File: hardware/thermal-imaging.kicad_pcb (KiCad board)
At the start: 2 copper layers, 40 x 40 mm, 47 parts, among them P1 CON-SENSOR, P2 Boot, P3 Debug, Q1 Oscillator, U1 XMC1XXX24, U10 DRILL, U11 DRILL, U2 74LVC1G17, U3 74LVC1G17, U4 FLIR-Lepton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

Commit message: specify oscillator frequency
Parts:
- Q1: value Oscillator -> 25MHz
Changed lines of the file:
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@@
-(kicad_pcb (version 4) (host pcbnew 4.0.2+dfsg1-stable)
+(kicad_pcb (version 4) (host pcbnew 4.0.6-e0-6349~52~ubuntu16.10.1)
   (general
     (links 145)
     (no_connects 0)
-    (area 166.324999 80.824999 206.475001 120.975001)
+    (area 165.544999 80.044999 282.34286 161.24)
     (thickness 1.6)
     (drawings 12)
@@
       (effects (font (size 0.3 0.3) (thickness 0.075)))
     )
-    (fp_text value Oscillator (at 0 -0.5 270) (layer F.Fab)
+    (fp_text value 25MHz (at 0 -0.5 270) (layer F.Fab)
       (effects (font (size 0.3 0.3) (thickness 0.075)))
     )

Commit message: specify filter circuit
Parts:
- C16: value TBD -> 220pF
- RP1: value TBD -> 82
- U7: value MCP1700T-1202E/TT -> MCP1700T-1202E/TT
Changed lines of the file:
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@@
-(kicad_pcb (version 4) (host pcbnew 4.0.6-e0-6349~52~ubuntu16.10.1)
+(kicad_pcb (version 4) (host pcbnew 4.0.7-e0-6372~58~ubuntu16.10.1)
   (general
     (links 145)
     (no_connects 0)
-    (area 165.544999 80.044999 282.34286 161.24)
+    (area 166.324999 80.824999 206.475001 120.975001)
     (thickness 1.6)
     (drawings 12)
@@
       (effects (font (size 0.3 0.3) (thickness 0.075)))
     )
-    (fp_text value " MCP1700T-1202E/TT " (at -0.775 -1.15) (layer F.Fab)
+    (fp_text value MCP1700T-1202E/TT (at -0.775 -1.15) (layer F.Fab)
       (effects (font (size 0.29972 0.29972) (thickness 0.07112)))
     )
@@
       (effects (font (size 0.2 0.2) (thickness 0.05)))
     )
-    (fp_text value TBD (at -0.025 -0.45 225) (layer F.Fab)
+    (fp_text value 82 (at -0.025 -0.45 225) (layer F.Fab)
       (effects (font (size 0.2 0.2) (thickness 0.05)))
     )
@@
       (effects (font (size 0.2 0.2) (thickness 0.05)))
     )
-    (fp_text value TBD (at 0 -0.275 315) (layer F.Fab)
+    (fp_text value 220pF (at 0 -0.275 315) (layer F.Fab)
       (effects (font (size 0.2 0.2) (thickness 0.05)))
     )

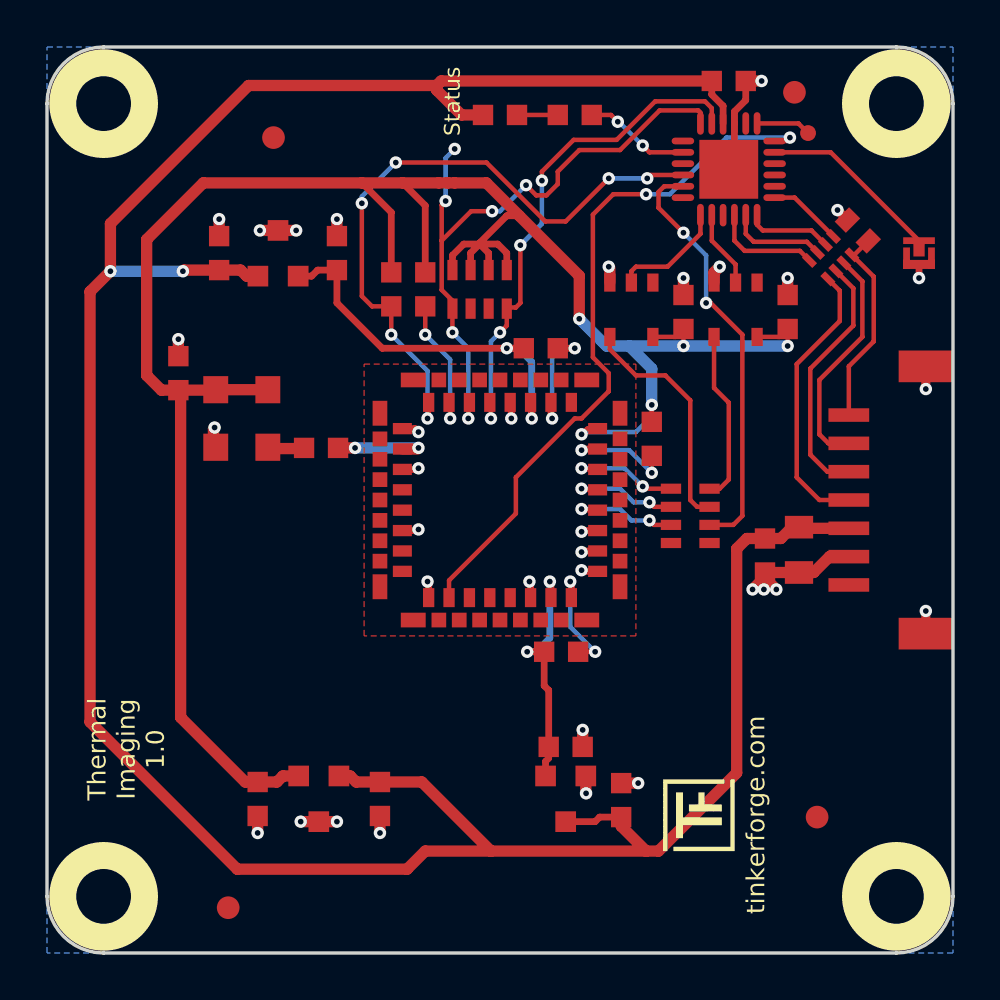
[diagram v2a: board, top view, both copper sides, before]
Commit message: add flir logo
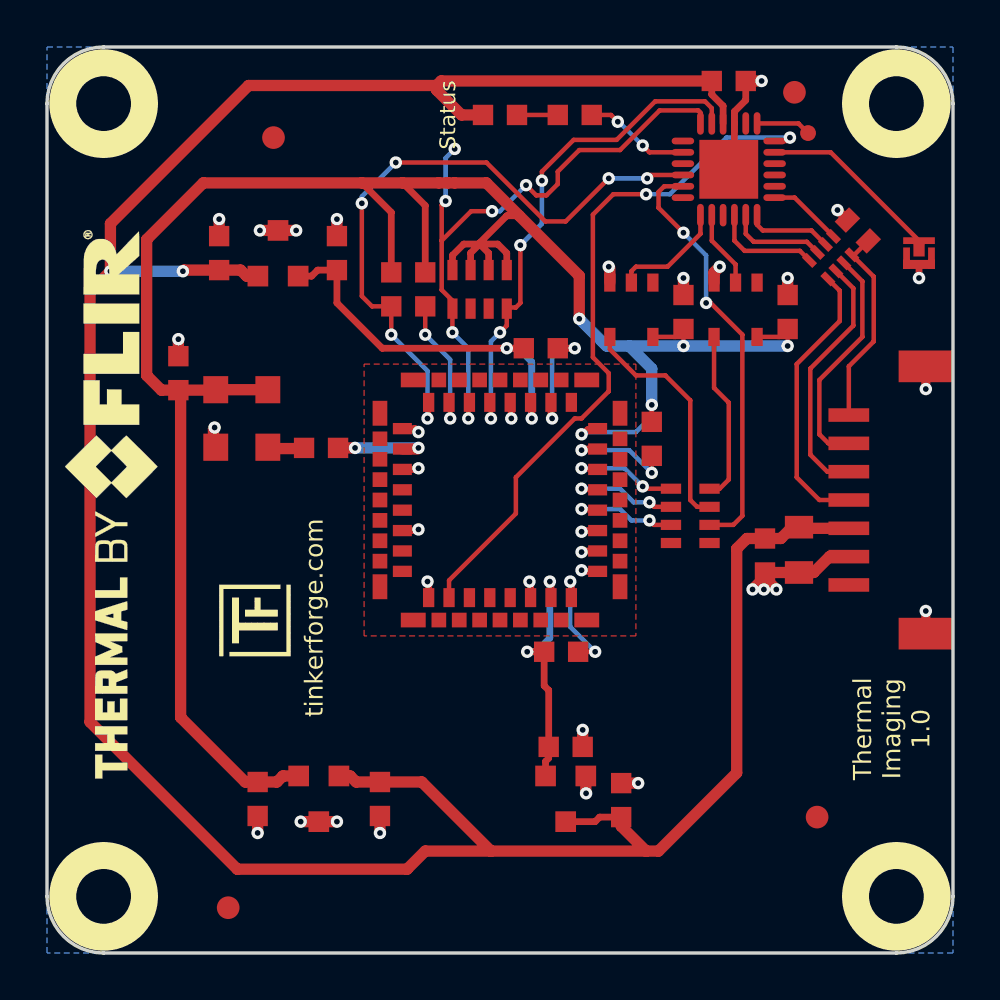
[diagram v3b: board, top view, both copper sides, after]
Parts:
- added G***: LOGO, kicad-libraries:logo_therm_by_flir, F.Cu at (169.2, 100.9)
- U5, U6: value AP7333-28 -> AP7333-28SAG
- moved G*** 21.4 mm to (174.0, 107.8)

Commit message: specify processor type
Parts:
- U1: value XMC1XXX24 -> XMC1302-32
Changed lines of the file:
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@@
     (links 145)
     (no_connects 0)
-    (area 166.324999 80.824999 206.475001 120.975001)
+    (area 165.544999 80.044999 282.34286 161.24)
     (thickness 1.6)
     (drawings 12)
@@
       (effects (font (size 0.3 0.3) (thickness 0.075)))
     )
-    (fp_text value XMC1XXX24 (at 0 0.8 180) (layer F.Fab)
+    (fp_text value XMC1302-32 (at 0 0.8 180) (layer F.Fab)
       (effects (font (size 0.3 0.3) (thickness 0.075)))
     )

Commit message: Add 3d information (tbc)
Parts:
- C16: footprint C0402E -> kicad-libraries:C0402E
- P3: footprint DEBUG_PAD -> kicad-libraries:DEBUG_PAD
